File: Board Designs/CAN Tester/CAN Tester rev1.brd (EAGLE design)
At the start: 160 x 100 mm, 21 parts, among them M1 Minifit, M2 Nanofit, U1 ISOLATED CAN TERMINAL, U2 TERMINATION_RESISTOR_JUMPER, U3 TEENSY_3.2_SIMPLE, U4 CHARACTER_LCD

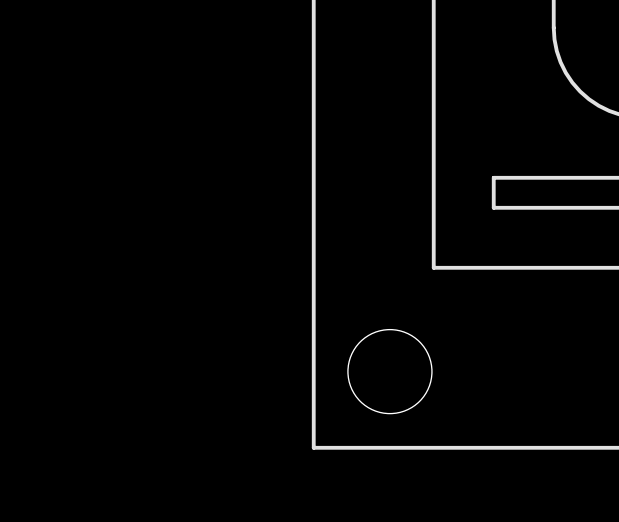
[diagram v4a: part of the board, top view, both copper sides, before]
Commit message: Added nets between all compnenets except LCD. Added 5 volt regulator.
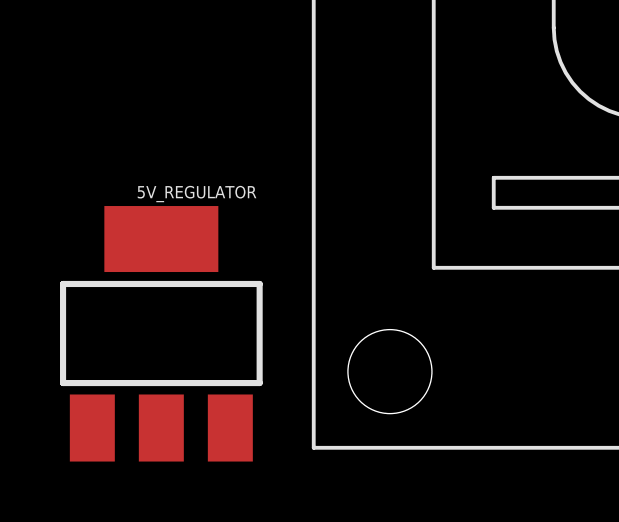
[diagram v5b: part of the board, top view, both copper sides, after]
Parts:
- added 5V_REGULATOR: (no value), HyTechDevices:SOT223
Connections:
- new net +3V3: MODE_SWITCH.B1, MODE_SWITCH.B2, SPARE_BUTTON.B1, SPARE_BUTTON.B2, U3.3.3V
- new net +5V: 5V_REGULATOR.3, U1.P$1, U1.P$8, U3.VIN
- new net CANH: U1.P$7, U2.1
- new net CANL: CAN_TERMINATION_RESISTOR.1, CAN_TERMINATION_RESISTOR.2, M1.3, M2.3, U1.P$6, U2.2
- new net CANRX: U1.P$2, U3.D4(CANRX)
- new net CANTX: M1.2, M2.2, U1.P$3, U3.D3(CANTX)
- new net GND: 5V_REGULATOR.2, 5V_REGULATOR.4, ACKERR.C, INCOMING.C, LINE_OK.C, M1.1, M2.1, OUTGOING.C, R_SPARE_BUTTON.2, SPARE.C, U3.GND
- new net N$10: OUTGOING.A, R2.1
- new net N$11: INCOMING.A, R1.1
- new net N$12: R_SPARE_BUTTON.1, SPARE_BUTTON.A2
- new net N$13: MODE_SWITCH.A1, U3.A6
- new net N$14: MODE_SWITCH.A2, R_MODE_SWITCH.1
- new net N$15: R_MODE_SWITCH.2
- new net N$16: U1.P$4, U1.P$5
- new net N$2: R5.1, SPARE.A
- new net N$3: SPARE_BUTTON.A1, U3.A5
- new net N$4: R2.2, U3.A1
- new net N$5: R3.2, U3.A2
- new net N$6: R4.2, U3.A3
- new net N$7: R5.2, U3.A4
- new net N$8: LINE_OK.A, R4.1
- new net N$9: ACKERR.A, R3.1
- new net VIN: 5V_REGULATOR.1, M1.4, M2.4
- net N$1: now also R1.2, U3.A0; no longer CAN_TERMINATION_RESISTOR.1, U2.2
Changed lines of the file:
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@@
 <element name="M1" library="HyTechDevices" package="DURACLIK_RIGHT_ANGLE-4" value="Minifit" x="-96.52" y="-123.19"/>
 <element name="U4" library="HyTechDevices" package="LCD1602" value="CHARACTER_LCD" x="-102.87" y="-161.29"/>
+<element name="5V_REGULATOR" library="HyTechDevices" package="SOT223" value="" x="-107.95" y="-157.48"/>
 </elements>
 <signals>
-<signal name="N$1">
+<signal name="CANTX">
+<contactref element="M2" pad="2"/>
+<contactref element="M1" pad="2"/>
+<contactref element="U3" pad="D3(CANTX)"/>
+<contactref element="U1" pad="P$3"/>
+<wire x1="-100.31" y1="-101.6" x2="-95.52" y2="-115.06" width="0" layer="19" extent="1-1"/>
+<wire x1="-29.21" y1="-35.28" x2="-100.31" y2="-101.6" width="0" layer="19" extent="1-1"/>
+<wire x1="-17.78" y1="25.4" x2="-29.21" y2="-35.28" width="0" layer="19" extent="1-1"/>
+</signal>
+<signal name="CANL">
+<contactref element="M2" pad="3"/>
+<contactref element="M1" pad="3"/>
+<contactref element="U1" pad="P$6"/>
 <contactref element="CAN_TERMINATION_RESISTOR" pad="1"/>
 <contactref element="U2" pad="2"/>
-<wire x1="-90.415" y1="-91.44" x2="-92.465" y2="-93.98" width="0" layer="19" extent="1-1"/>
+<contactref element="CAN_TERMINATION_RESISTOR" pad="2"/>
+<wire x1="-97.81" y1="-98.3" x2="-97.52" y2="-115.06" width="0" layer="19" extent="1-1"/>
+<wire x1="-92.465" y1="-93.98" x2="-97.81" y2="-98.3" width="0" layer="19" extent="1-1"/>
+<wire x1="-90.415" y1="-93.98" x2="-92.465" y2="-93.98" width="0" layer="19" extent="1-1"/>
+<wire x1="-90.415" y1="-91.44" x2="-90.415" y2="-93.98" width="0" layer="19" extent="1-1"/>
+<wire x1="-29.21" y1="-25.68" x2="-90.415" y2="-91.44" width="0" layer="19" extent="1-1"/>
+</signal>
+<signal name="GND">
+<contactref element="U3" pad="GND"/>
+<contactref element="M2" pad="1"/>
+<contactref element="M1" pad="1"/>
+<contactref element="5V_REGULATOR" pad="2"/>
+<contactref element="5V_REGULATOR" pad="4"/>
+<contactref element="SPARE" pad="C"/>
+<contactref element="LINE_OK" pad="C"/>
+<contactref element="ACKERR" pad="C"/>
+<contactref element="OUTGOING" pad="C"/>
+<contactref element="INCOMING" pad="C"/>
+<contactref element="R_SPARE_BUTTON" pad="2"/>
+<wire x1="-90.415" y1="-111.76" x2="-93.52" y2="-115.06" width="0" layer="19" extent="1-1"/>
+<wire x1="-97.81" y1="-101.6" x2="-90.415" y2="-111.76" width="0" layer="19" extent="1-1"/>
+<wire x1="-90.17" y1="-71.34" x2="-97.81" y2="-101.6" width="0" layer="19" extent="1-1"/>
+<wire x1="-83.82" y1="-71.34" x2="-90.17" y2="-71.34" width="0" layer="19" extent="1-1"/>
+<wire x1="-77.47" y1="-71.34" x2="-83.82" y2="-71.34" width="0" layer="19" extent="1-1"/>
+<wire x1="-71.12" y1="-71.34" x2="-77.47" y2="-71.34" width="0" layer="19" extent="1-1"/>
+<wire x1="-64.77" y1="-71.34" x2="-71.12" y2="-71.34" width="0" layer="19" extent="1-1"/>
+<wire x1="-107.95" y1="-154.33" x2="-93.52" y2="-115.06" width="0" layer="19" extent="1-1"/>
+<wire x1="-107.95" y1="-160.63" x2="-107.95" y2="-154.33" width="0" layer="19" extent="1-1"/>
+<wire x1="-17.78" y1="35.56" x2="-64.77" y2="-71.34" width="0" layer="19" extent="1-1"/>
+</signal>
+<signal name="VIN">
+<contactref element="M2" pad="4"/>
+<contactref element="M1" pad="4"/>
+<contactref element="5V_REGULATOR" pad="1"/>
+<wire x1="-100.31" y1="-98.3" x2="-99.52" y2="-115.06" width="0" layer="19" extent="1-1"/>
+<wire x1="-110.25" y1="-160.63" x2="-99.52" y2="-115.06" width="0" layer="19" extent="1-1"/>
+</signal>
+<signal name="CANH">
+<contactref element="U1" pad="P$7"/>
+<contactref element="U2" pad="1"/>
+<wire x1="-31.75" y1="-25.68" x2="-92.465" y2="-91.44" width="0" layer="19" extent="1-1"/>
+</signal>
+<signal name="CANRX">
+<contactref element="U3" pad="D4(CANRX)"/>
+<contactref element="U1" pad="P$2"/>
+<wire x1="-17.78" y1="22.86" x2="-31.75" y2="-35.28" width="0" layer="19" extent="1-1"/>
+</signal>
+<signal name="N$2">
+<contactref element="R5" pad="1"/>
+<contactref element="SPARE" pad="A"/>
+<wire x1="-90.17" y1="-73.44" x2="-92.465" y2="-106.68" width="0" layer="19" extent="1-1"/>
+</signal>
+<signal name="N$1">
+<contactref element="U3" pad="A0"/>
+<contactref element="R1" pad="2"/>
+<wire x1="-2.54" y1="5.08" x2="-90.415" y2="-96.52" width="0" layer="19" extent="1-1"/>
+</signal>
+<signal name="N$4">
+<contactref element="U3" pad="A1"/>
+<contactref element="R2" pad="2"/>
+<wire x1="-2.54" y1="7.62" x2="-90.415" y2="-99.06" width="0" layer="19" extent="1-1"/>
+</signal>
+<signal name="N$5">
+<contactref element="U3" pad="A2"/>
+<contactref element="R3" pad="2"/>
+<wire x1="-2.54" y1="10.16" x2="-90.415" y2="-101.6" width="0" layer="19" extent="1-1"/>
+</signal>
+<signal name="N$6">
+<contactref element="U3" pad="A3"/>
+<contactref element="R4" pad="2"/>
+<wire x1="-2.54" y1="12.7" x2="-90.415" y2="-104.14" width="0" layer="19" extent="1-1"/>
+</signal>
+<signal name="N$7">
+<contactref element="U3" pad="A4"/>
+<contactref element="R5" pad="2"/>
+<wire x1="-2.54" y1="15.24" x2="-90.415" y2="-106.68" width="0" layer="19" extent="1-1"/>
+</signal>
+<signal name="N$8">
+<contactref element="R4" pad="1"/>
+<contactref element="LINE_OK" pad="A"/>
+<wire x1="-83.82" y1="-73.44" x2="-92.465" y2="-104.14" width="0" layer="19" extent="1-1"/>
+</signal>
+<signal name="N$9">
+<contactref element="R3" pad="1"/>
+<contactref element="ACKERR" pad="A"/>
+<wire x1="-77.47" y1="-73.44" x2="-92.465" y2="-101.6" width="0" layer="19" extent="1-1"/>
+</signal>
+<signal name="N$10">
+<contactref element="R2" pad="1"/>
+<contactref element="OUTGOING" pad="A"/>
+<wire x1="-71.12" y1="-73.44" x2="-92.465" y2="-99.06" width="0" layer="19" extent="1-1"/>
+</signal>
+<signal name="N$11">
+<contactref element="R1" pad="1"/>
+<contactref element="INCOMING" pad="A"/>
+<wire x1="-64.77" y1="-73.44" x2="-92.465" y2="-96.52" width="0" layer="19" extent="1-1"/>
+</signal>
+<signal name="N$3">
+<contactref element="U3" pad="A5"/>
+<contactref element="SPARE_BUTTON" pad="A1"/>
+<wire x1="-2.54" y1="17.78" x2="-91.605" y2="-88.61" width="0" layer="19" extent="1-1"/>
+</signal>
+<signal name="N$12">
+<contactref element="SPARE_BUTTON" pad="A2"/>
+<contactref element="R_SPARE_BUTTON" pad="1"/>
+<wire x1="-83.655" y1="-88.61" x2="-92.465" y2="-111.76" width="0" layer="19" extent="1-1"/>
+</signal>
+<signal name="+3V3">
+<contactref element="SPARE_BUTTON" pad="B2"/>
+<contactref element="U3" pad="3.3V"/>
+<contactref element="SPARE_BUTTON" pad="B1"/>
+<contactref element="MODE_SWITCH" pad="B1"/>
+<contactref element="MODE_SWITCH" pad="B2"/>
+<wire x1="-91.605" y1="-76.49" x2="-91.605" y2="-84.11" width="0" layer="19" extent="1-1"/>
+<wire x1="-83.655" y1="-84.11" x2="-91.605" y2="-84.11" width="0" layer="19" extent="1-1"/>
+<wire x1="-83.655" y1="-76.49" x2="-83.655" y2="-84.11" width="0" layer="19" extent="1-1"/>
+<wire x1="-2.54" y1="30.48" x2="-83.655" y2="-76.49" width="0" layer="19" extent="1-1"/>
+</signal>
+<signal name="+5V">
+<contactref element="U3" pad="VIN"/>
+<contactref element="5V_REGULATOR" pad="3"/>
+<contactref element="U1" pad="P$1"/>
+<contactref element="U1" pad="P$8"/>
+<wire x1="-34.29" y1="-25.68" x2="-34.29" y2="-35.28" width="0" layer="19" extent="1-1"/>
+<wire x1="-2.54" y1="35.56" x2="-34.29" y2="-25.68" width="0" layer="19" extent="1-1"/>
+<wire x1="-105.65" y1="-160.63" x2="-34.29" y2="-35.28" width="0" layer="19" extent="1-1"/>
+</signal>
+<signal name="N$13">
+<contactref element="U3" pad="A6"/>
+<contactref element="MODE_SWITCH" pad="A1"/>
+<wire x1="-2.54" y1="20.32" x2="-91.605" y2="-80.99" width="0" layer="19" extent="1-1"/>
+</signal>
+<signal name="N$14">
+<contactref element="MODE_SWITCH" pad="A2"/>
+<contactref element="R_MODE_SWITCH" pad="1"/>
+<wire x1="-83.655" y1="-80.99" x2="-92.465" y2="-109.22" width="0" layer="19" extent="1-1"/>
+</signal>
+<signal name="N$15">
+<contactref element="R_MODE_SWITCH" pad="2"/>
+</signal>
+<signal name="N$16">
+<contactref element="U1" pad="P$5"/>
+<contactref element="U1" pad="P$4"/>
+<wire x1="-26.67" y1="-25.68" x2="-26.67" y2="-35.28" width="0" layer="19" extent="1-1"/>
 </signal>
 </signals>

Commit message: Small changes with schematic
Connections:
- net +3V3: now also U4.2
- net +5V: now also U4.15
- net GND: now also U4.1, U4.16
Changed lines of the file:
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@@
 <contactref element="INCOMING" pad="C"/>
 <contactref element="R_SPARE_BUTTON" pad="2"/>
+<contactref element="U4" pad="1"/>
+<contactref element="U4" pad="16"/>
+<wire x1="-93.52" y1="-115.06" x2="-94.87" y2="-127.83" width="0" layer="19" extent="1-1"/>
 <wire x1="-90.415" y1="-111.76" x2="-93.52" y2="-115.06" width="0" layer="19" extent="1-1"/>
 <wire x1="-97.81" y1="-101.6" x2="-90.415" y2="-111.76" width="0" layer="19" extent="1-1"/>
+<wire x1="-107.95" y1="-154.33" x2="-94.87" y2="-127.83" width="0" layer="19" extent="1-1"/>
+<wire x1="-107.95" y1="-160.63" x2="-107.95" y2="-154.33" width="0" layer="19" extent="1-1"/>
 <wire x1="-90.17" y1="-71.34" x2="-97.81" y2="-101.6" width="0" layer="19" extent="1-1"/>
 <wire x1="-83.82" y1="-71.34" x2="-90.17" y2="-71.34" width="0" layer="19" extent="1-1"/>
@@
 <wire x1="-71.12" y1="-71.34" x2="-77.47" y2="-71.34" width="0" layer="19" extent="1-1"/>
 <wire x1="-64.77" y1="-71.34" x2="-71.12" y2="-71.34" width="0" layer="19" extent="1-1"/>
-<wire x1="-107.95" y1="-154.33" x2="-93.52" y2="-115.06" width="0" layer="19" extent="1-1"/>
-<wire x1="-107.95" y1="-160.63" x2="-107.95" y2="-154.33" width="0" layer="19" extent="1-1"/>
+<wire x1="-56.77" y1="-127.83" x2="-90.415" y2="-111.76" width="0" layer="19" extent="1-1"/>
 <wire x1="-17.78" y1="35.56" x2="-64.77" y2="-71.34" width="0" layer="19" extent="1-1"/>
 </signal>
@@
 <contactref element="MODE_SWITCH" pad="B1"/>
 <contactref element="MODE_SWITCH" pad="B2"/>
+<contactref element="U4" pad="2"/>
+<wire x1="-91.605" y1="-84.11" x2="-92.33" y2="-127.83" width="0" layer="19" extent="1-1"/>
 <wire x1="-91.605" y1="-76.49" x2="-91.605" y2="-84.11" width="0" layer="19" extent="1-1"/>
 <wire x1="-83.655" y1="-84.11" x2="-91.605" y2="-84.11" width="0" layer="19" extent="1-1"/>
@@
 <contactref element="U1" pad="P$1"/>
 <contactref element="U1" pad="P$8"/>
+<contactref element="U4" pad="15"/>
+<wire x1="-105.65" y1="-160.63" x2="-59.31" y2="-127.83" width="0" layer="19" extent="1-1"/>
+<wire x1="-34.29" y1="-35.28" x2="-59.31" y2="-127.83" width="0" layer="19" extent="1-1"/>
 <wire x1="-34.29" y1="-25.68" x2="-34.29" y2="-35.28" width="0" layer="19" extent="1-1"/>
 <wire x1="-2.54" y1="35.56" x2="-34.29" y2="-25.68" width="0" layer="19" extent="1-1"/>
-<wire x1="-105.65" y1="-160.63" x2="-34.29" y2="-35.28" width="0" layer="19" extent="1-1"/>
 </signal>
 <signal name="N$13">

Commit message: Finished schematic - need to verify
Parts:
- added CONTRAST_POT: 10k, HyTechDevices:TRIM-3386
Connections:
- new net N$17: U3.D5, U4.4
- new net N$18: U3.D6, U4.6
- new net N$19: U3.D7(RX3), U4.11
- new net N$20: U3.D8(TX3), U4.12
- new net N$21: U3.D9(RX2), U4.13
- new net N$22: U3.D10(TX2), U4.14
- new net VO: CONTRAST_POT.2, U4.3
- new net VSS: U4.1
- net +5V: now also CONTRAST_POT.3
- net GND: now also CONTRAST_POT.1, U4.5; no longer U4.1
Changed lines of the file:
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@@
 <element name="U4" library="HyTechDevices" package="LCD1602" value="CHARACTER_LCD" x="-102.87" y="-161.29"/>
 <element name="5V_REGULATOR" library="HyTechDevices" package="SOT223" value="" x="-107.95" y="-157.48"/>
+<element name="CONTRAST_POT" library="HyTechDevices" package="TRIM-3386" value="10k" x="-104.14" y="-167.64"/>
 </elements>
 <signals>
@@
 <contactref element="INCOMING" pad="C"/>
 <contactref element="R_SPARE_BUTTON" pad="2"/>
-<contactref element="U4" pad="1"/>
+<contactref element="CONTRAST_POT" pad="1"/>
+<contactref element="U4" pad="5"/>
 <contactref element="U4" pad="16"/>
-<wire x1="-93.52" y1="-115.06" x2="-94.87" y2="-127.83" width="0" layer="19" extent="1-1"/>
+<wire x1="-93.52" y1="-115.06" x2="-84.71" y2="-127.83" width="0" layer="19" extent="1-1"/>
 <wire x1="-90.415" y1="-111.76" x2="-93.52" y2="-115.06" width="0" layer="19" extent="1-1"/>
 <wire x1="-97.81" y1="-101.6" x2="-90.415" y2="-111.76" width="0" layer="19" extent="1-1"/>
-<wire x1="-107.95" y1="-154.33" x2="-94.87" y2="-127.83" width="0" layer="19" extent="1-1"/>
-<wire x1="-107.95" y1="-160.63" x2="-107.95" y2="-154.33" width="0" layer="19" extent="1-1"/>
+<wire x1="-56.77" y1="-127.83" x2="-84.71" y2="-127.83" width="0" layer="19" extent="1-1"/>
 <wire x1="-90.17" y1="-71.34" x2="-97.81" y2="-101.6" width="0" layer="19" extent="1-1"/>
 <wire x1="-83.82" y1="-71.34" x2="-90.17" y2="-71.34" width="0" layer="19" extent="1-1"/>
@@
 <wire x1="-71.12" y1="-71.34" x2="-77.47" y2="-71.34" width="0" layer="19" extent="1-1"/>
 <wire x1="-64.77" y1="-71.34" x2="-71.12" y2="-71.34" width="0" layer="19" extent="1-1"/>
-<wire x1="-56.77" y1="-127.83" x2="-90.415" y2="-111.76" width="0" layer="19" extent="1-1"/>
+<wire x1="-107.95" y1="-154.33" x2="-84.71" y2="-127.83" width="0" layer="19" extent="1-1"/>
+<wire x1="-107.95" y1="-160.63" x2="-107.95" y2="-154.33" width="0" layer="19" extent="1-1"/>
+<wire x1="-106.68" y1="-170.4975" x2="-107.95" y2="-160.63" width="0" layer="19" extent="1-1"/>
 <wire x1="-17.78" y1="35.56" x2="-64.77" y2="-71.34" width="0" layer="19" extent="1-1"/>
 </signal>
@@
 <contactref element="U1" pad="P$8"/>
 <contactref element="U4" pad="15"/>
+<contactref element="CONTRAST_POT" pad="3"/>
 <wire x1="-105.65" y1="-160.63" x2="-59.31" y2="-127.83" width="0" layer="19" extent="1-1"/>
+<wire x1="-101.6" y1="-170.4975" x2="-105.65" y2="-160.63" width="0" layer="19" extent="1-1"/>
 <wire x1="-34.29" y1="-35.28" x2="-59.31" y2="-127.83" width="0" layer="19" extent="1-1"/>
 <wire x1="-34.29" y1="-25.68" x2="-34.29" y2="-35.28" width="0" layer="19" extent="1-1"/>
@@
 <wire x1="-26.67" y1="-25.68" x2="-26.67" y2="-35.28" width="0" layer="19" extent="1-1"/>
 </signal>
+<signal name="VO">
+<contactref element="CONTRAST_POT" pad="2"/>
+<contactref element="U4" pad="3"/>
+<wire x1="-104.14" y1="-170.4975" x2="-89.79" y2="-127.83" width="0" layer="19" extent="1-1"/>
+</signal>
+<signal name="VSS">
+<contactref element="U4" pad="1"/>
+</signal>
+<signal name="N$17">
+<contactref element="U4" pad="4"/>
+<contactref element="U3" pad="D5"/>
+<wire x1="-17.78" y1="20.32" x2="-87.25" y2="-127.83" width="0" layer="19" extent="1-1"/>
+</signal>
+<signal name="N$18">
+<contactref element="U4" pad="6"/>
+<contactref element="U3" pad="D6"/>
+<wire x1="-17.78" y1="17.78" x2="-82.17" y2="-127.83" width="0" layer="19" extent="1-1"/>
+</signal>
+<signal name="N$19">
+<contactref element="U4" pad="11"/>
+<contactref element="U3" pad="D7(RX3)"/>
+<wire x1="-17.78" y1="15.24" x2="-69.47" y2="-127.83" width="0" layer="19" extent="1-1"/>
+</signal>
+<signal name="N$20">
+<contactref element="U4" pad="12"/>
+<contactref element="U3" pad="D8(TX3)"/>
+<wire x1="-17.78" y1="12.7" x2="-66.93" y2="-127.83" width="0" layer="19" extent="1-1"/>
+</signal>
+<signal name="N$21">
+<contactref element="U4" pad="13"/>
+<contactref element="U3" pad="D9(RX2)"/>
+<wire x1="-17.78" y1="10.16" x2="-64.39" y2="-127.83" width="0" layer="19" extent="1-1"/>
+</signal>
+<signal name="N$22">
+<contactref element="U4" pad="14"/>
+<contactref element="U3" pad="D10(TX2)"/>
+<wire x1="-17.78" y1="7.62" x2="-61.85" y2="-127.83" width="0" layer="19" extent="1-1"/>
+</signal>
 </signals>
